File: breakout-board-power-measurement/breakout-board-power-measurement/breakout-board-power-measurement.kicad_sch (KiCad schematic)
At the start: 59 parts, among them J1 Screw_Terminal_01x04, J2 Conn_01x07, J3 Conn_01x07, Q1 NMOS, Q2 NMOS, U1 MCP3911A0-E/SS, U2 Si8641BA-B-IU, U3 LM317_3PinPackage, Y1 10M

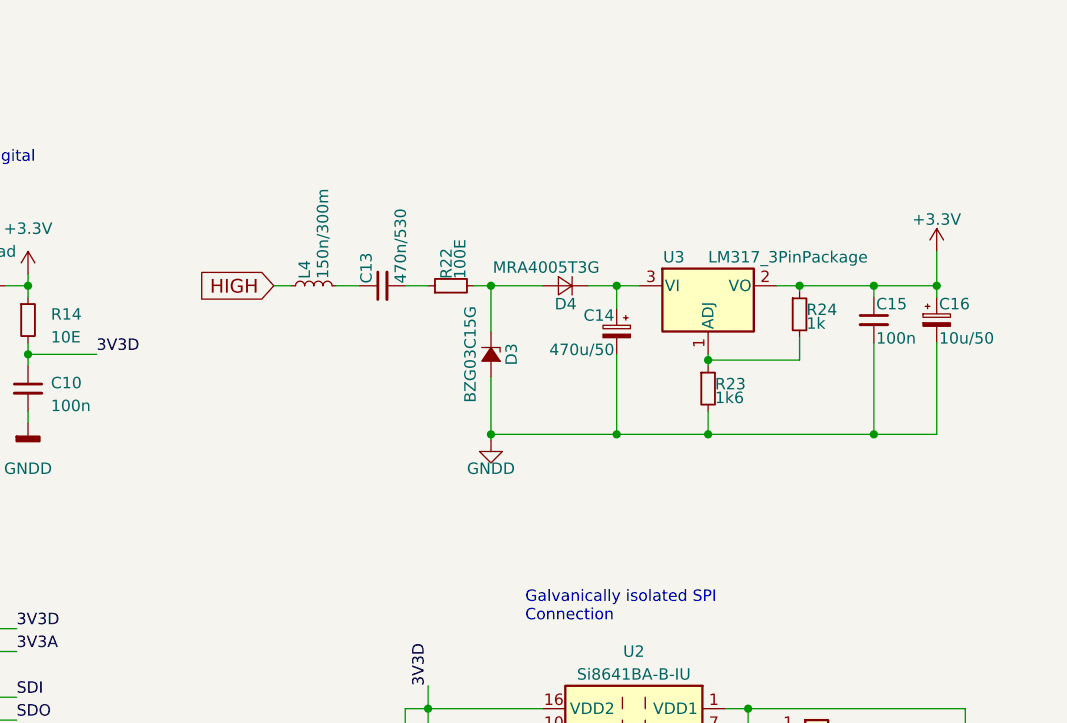
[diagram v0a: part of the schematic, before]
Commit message: LTSpice .raw files wont be uploaded any more. power-measurement breakout will be finished tomorrow
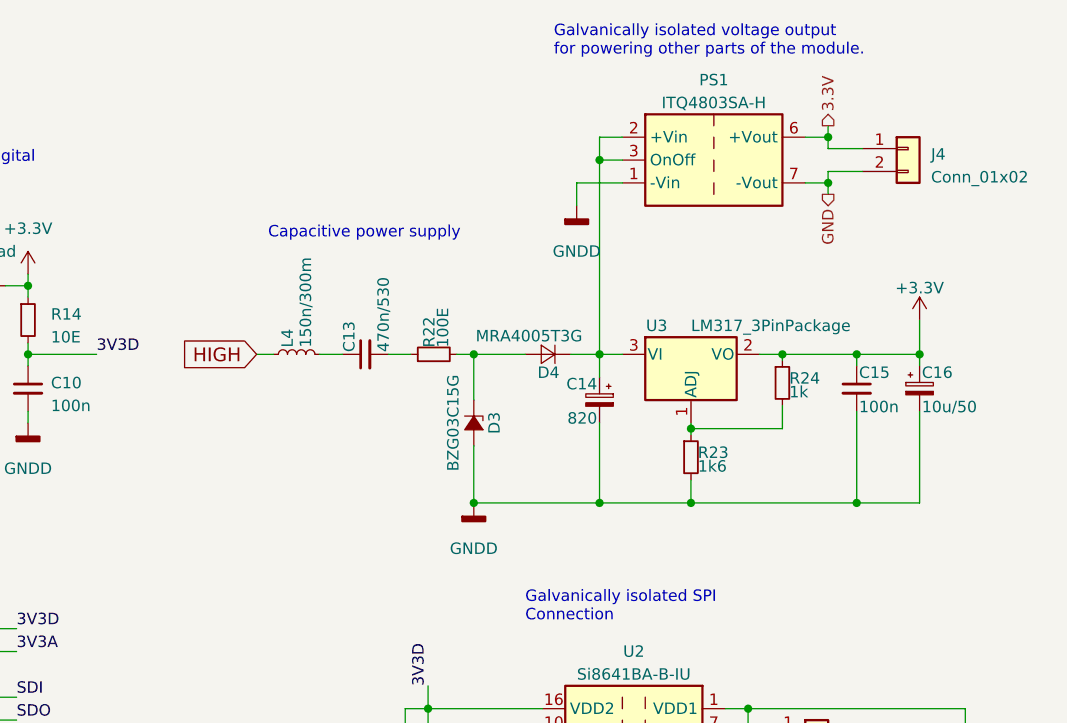
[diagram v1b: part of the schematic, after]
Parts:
- added J4: Conn_01x02, symbol Connector_Generic:Conn_01x02
- added PS1: ITQ4803SA-H, Converter_DCDC:Converter_DCDC_XP_POWER-ITQxxxxS-H_THT, symbol Converter_DCDC:ITQ4803SA-H
- C14: value 470u/50 -> 820
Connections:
- net GNDD: now also PS1.1 (-Vin)
- net at C14.1, D4.1 (K), U3.3 (VI): now also PS1.2 (+Vin), PS1.3 (OnOff)
- new net 3.3V: J4.1 (Pin_1), PS1.6 (+Vout)
- new net GND: J4.2 (Pin_2), PS1.7 (-Vout)
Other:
- note added: "Capacitive power supply"
- note added: "Galvanically isolated voltage output for powering other parts of the module."
- moved on the sheet: C13, C14, C15, C16, D3, D4, L4, R22, R23, R24, U3

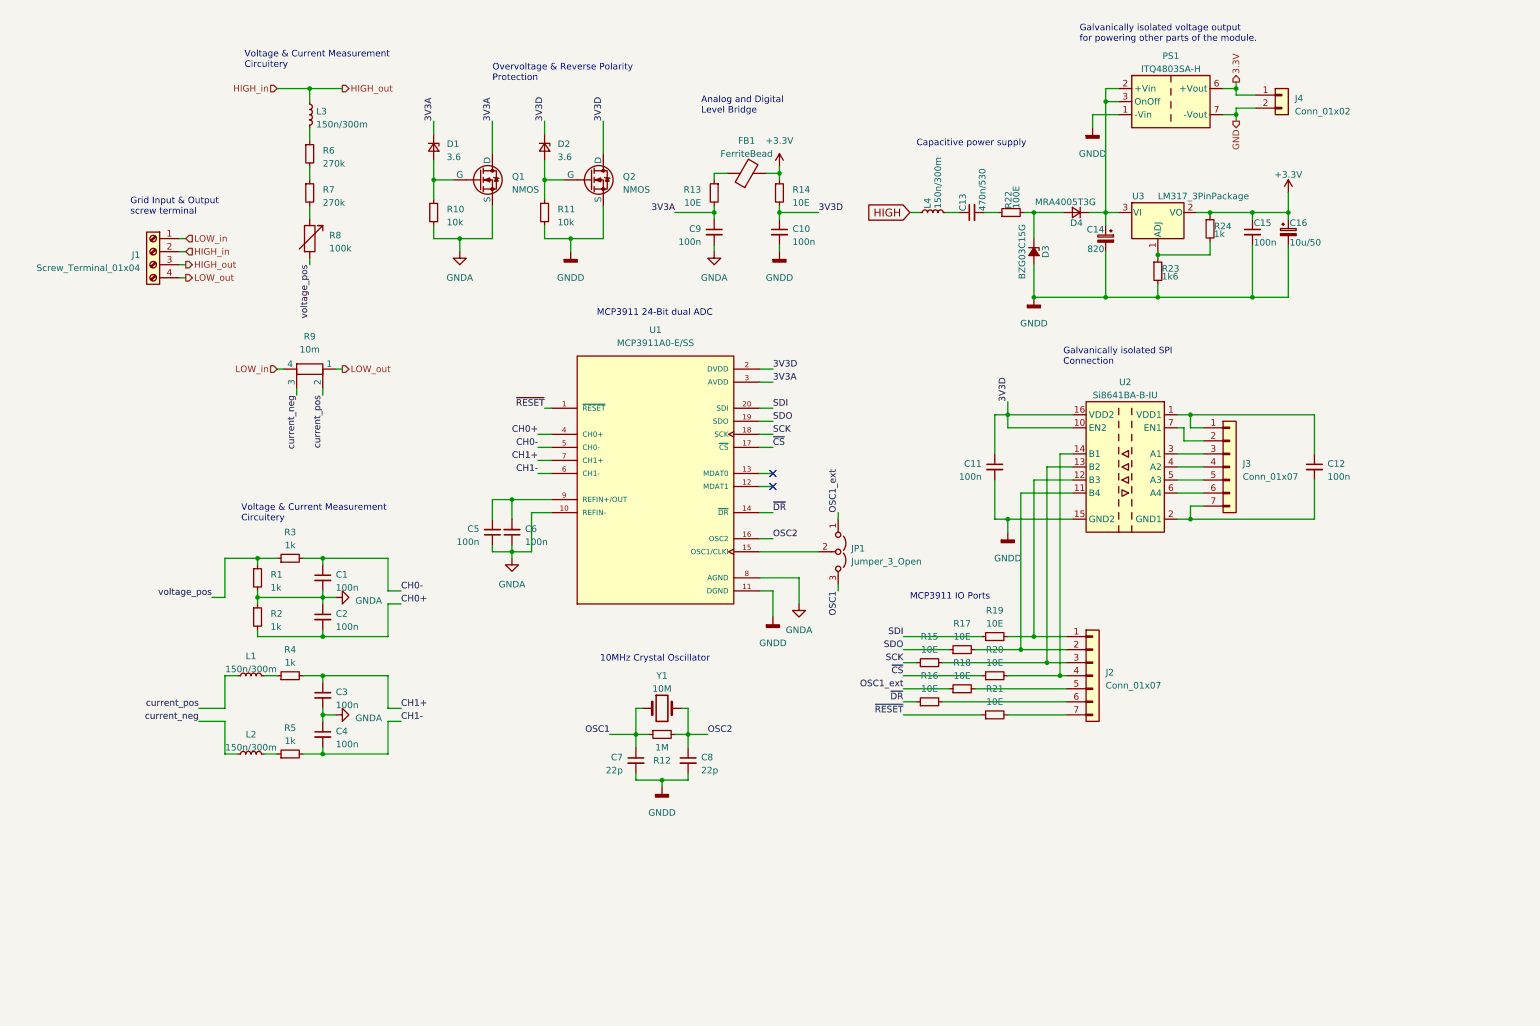
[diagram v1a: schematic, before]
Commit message: power measurement schematic organized
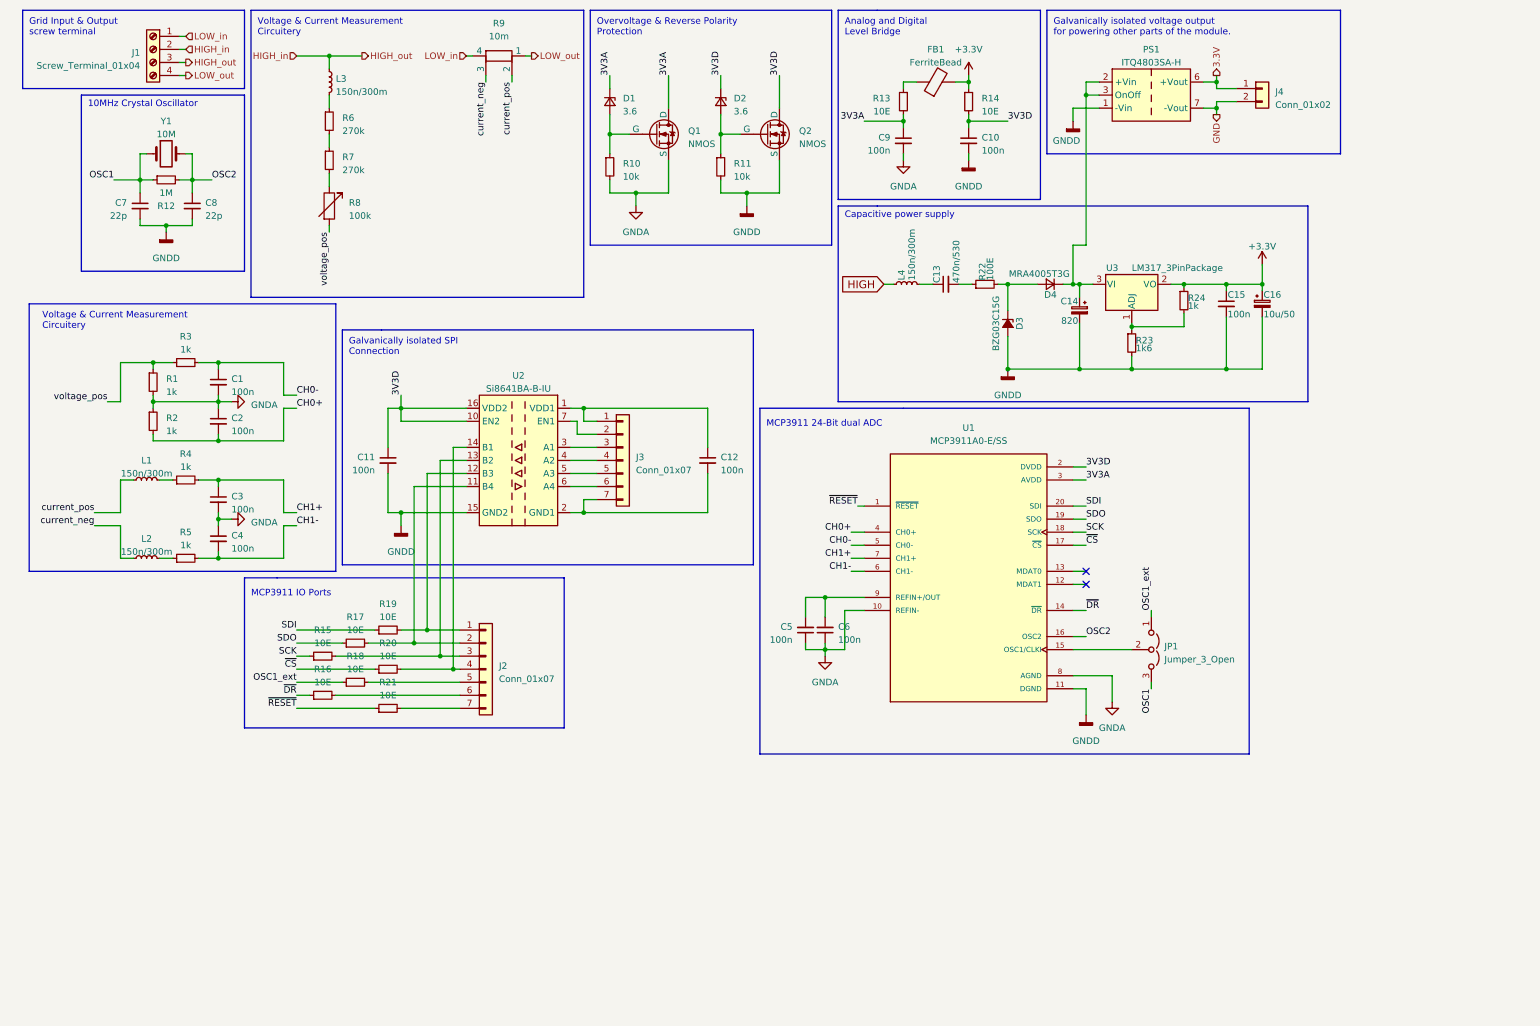
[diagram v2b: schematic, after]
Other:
- moved on the sheet: C1, C10, C11, C12, C13, C14, C15, C16, C2, C3, C4, C5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

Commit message: some footprints added
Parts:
- C1, C10, C11, C12, C2, C3, C4, C5, C6, C7, C8, C9: footprint (none) -> Capacitor_SMD:C_1206_3216Metric_Pad1.33x1.80mm_HandSolder
- J2, J3: footprint (none) -> Connector_PinSocket_2.54mm:PinSocket_1x07_P2.54mm_Vertical
- J4: footprint (none) -> Connector_PinSocket_2.54mm:PinSocket_1x02_P2.54mm_Vertical
- R1, R10, R11, R12, R13, R14, R15, R16, R17, R18, R19, R2, R20, R21, R3, R4, R5, R6, R7, R8: footprint (none) -> Resistor_SMD:R_1206_3216Metric_Pad1.30x1.75mm_HandSolder
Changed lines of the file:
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@@
       (effects (font (size 1.27 1.27)) (justify left))
     )
-    (property "Footprint" "" (at 128.27 44.45 0)
+    (property "Footprint" "Resistor_SMD:R_1206_3216Metric_Pad1.30x1.75mm_HandSolder" (at 128.27 44.45 0)
       (effects (font (size 1.27 1.27)) hide)
     )
@@
       (effects (font (size 1.27 1.27)) (justify left))
     )
-    (property "Footprint" "" (at 185.42 31.75 0)
+    (property "Footprint" "Resistor_SMD:R_1206_3216Metric_Pad1.30x1.75mm_HandSolder" (at 185.42 31.75 0)
       (effects (font (size 1.27 1.27)) hide)
     )
@@
       (effects (font (size 1.27 1.27)) (justify left))
     )
-    (property "Footprint" "" (at 149.86 44.45 0)
+    (property "Footprint" "Resistor_SMD:R_1206_3216Metric_Pad1.30x1.75mm_HandSolder" (at 149.86 44.45 0)
       (effects (font (size 1.27 1.27)) hide)
     )
@@
       (effects (font (size 1.27 1.27)) (justify left))
     )
-    (property "Footprint" "" (at 71.882 52.07 90)
+    (property "Footprint" "Resistor_SMD:R_1206_3216Metric_Pad1.30x1.75mm_HandSolder" (at 71.882 52.07 90)
       (effects (font (size 1.27 1.27)) hide)
     )
@@
       (effects (font (size 1.27 1.27)) (justify right))
     )
-    (property "Footprint" "" (at 170.18 134.62 0)
+    (property "Footprint" "Capacitor_SMD:C_1206_3216Metric_Pad1.33x1.80mm_HandSolder" (at 170.18 134.62 0)
       (effects (font (size 1.27 1.27)) hide)
     )
@@
       (effects (font (size 1.27 1.27)) (justify left))
     )
-    (property "Footprint" "" (at 36.83 52.07 0)
+    (property "Footprint" "Capacitor_SMD:C_1206_3216Metric_Pad1.33x1.80mm_HandSolder" (at 36.83 52.07 0)
       (effects (font (size 1.27 1.27)) hide)
     )
@@
       (effects (font (size 1.27 1.27)))
     )
-    (property "Footprint" "" (at 45.72 105.41 0)
+    (property "Footprint" "Resistor_SMD:R_1206_3216Metric_Pad1.30x1.75mm_HandSolder" (at 45.72 105.41 0)
       (effects (font (size 1.27 1.27)) hide)
     )
@@
       (effects (font (size 1.27 1.27)) (justify left))
     )
-    (property "Footprint" "" (at 73.66 35.56 0)
+    (property "Footprint" "Resistor_SMD:R_1206_3216Metric_Pad1.30x1.75mm_HandSolder" (at 73.66 35.56 0)
       (effects (font (size 1.27 1.27)) hide)
     )
@@
       (effects (font (size 1.27 1.27)) (justify left))
     )
-    (property "Footprint" "" (at 130.81 101.6 0)
+    (property "Footprint" "Connector_PinSocket_2.54mm:PinSocket_1x07_P2.54mm_Vertical" (at 130.81 101.6 0)
       (effects (font (size 1.27 1.27)) hide)
     )
@@
       (effects (font (size 1.27 1.27)) (justify left))
     )
-    (property "Footprint" "" (at 73.66 43.18 0)
+    (property "Footprint" "Resistor_SMD:R_1206_3216Metric_Pad1.30x1.75mm_HandSolder" (at 73.66 43.18 0)
       (effects (font (size 1.27 1.27)) hide)
     )
@@
       (effects (font (size 1.27 1.27)) (justify left))
     )
-    (property "Footprint" "" (at 104.14 142.24 0)
+    (property "Footprint" "Connector_PinSocket_2.54mm:PinSocket_1x07_P2.54mm_Vertical" (at 104.14 142.24 0)
       (effects (font (size 1.27 1.27)) hide)
     )
@@
       (effects (font (size 1.27 1.27)) (justify left))
     )
-    (property "Footprint" "" (at 46.99 52.07 0)
+    (property "Footprint" "Capacitor_SMD:C_1206_3216Metric_Pad1.33x1.80mm_HandSolder" (at 46.99 52.07 0)
       (effects (font (size 1.27 1.27)) hide)
     )
@@
       (effects (font (size 1.27 1.27)) (justify left))
     )
-    (property "Footprint" "" (at 39.37 93.98 0)
+    (property "Footprint" "Resistor_SMD:R_1206_3216Metric_Pad1.30x1.75mm_HandSolder" (at 39.37 93.98 0)
       (effects (font (size 1.27 1.27)) hide)
     )
@@
       (effects (font (size 1.27 1.27)) (justify left))
     )
-    (property "Footprint" "" (at 147.32 101.6 0)
+    (property "Footprint" "Capacitor_SMD:C_1206_3216Metric_Pad1.33x1.80mm_HandSolder" (at 147.32 101.6 0)
       (effects (font (size 1.27 1.27)) hide)
     )
@@
       (effects (font (size 1.27 1.27)))
     )
-    (property "Footprint" "" (at 78.74 137.16 0)
+    (property "Footprint" "Resistor_SMD:R_1206_3216Metric_Pad1.30x1.75mm_HandSolder" (at 78.74 137.16 0)
       (effects (font (size 1.27 1.27)) hide)
     )
@@
       (effects (font (size 1.27 1.27)))
     )
-    (property "Footprint" "" (at 45.72 120.65 0)
+    (property "Footprint" "Resistor_SMD:R_1206_3216Metric_Pad1.30x1.75mm_HandSolder" (at 45.72 120.65 0)
       (effects (font (size 1.27 1.27)) hide)
     )
@@
       (effects (font (size 1.27 1.27)) (justify left))
     )
-    (property "Footprint" "" (at 52.07 86.36 0)
+    (property "Footprint" "Capacitor_SMD:C_1206_3216Metric_Pad1.33x1.80mm_HandSolder" (at 52.07 86.36 0)
       (effects (font (size 1.27 1.27)) hide)
     )
@@
       (effects (font (size 1.27 1.27)) (justify left))
     )
-    (property "Footprint" "" (at 198.12 31.75 0)
+    (property "Footprint" "Resistor_SMD:R_1206_3216Metric_Pad1.30x1.75mm_HandSolder" (at 198.12 31.75 0)
       (effects (font (size 1.27 1.27)) hide)
     )
@@
       (effects (font (size 1.27 1.27)) (justify right))
     )
-    (property "Footprint" "" (at 166.37 134.62 0)
+    (property "Footprint" "Capacitor_SMD:C_1206_3216Metric_Pad1.33x1.80mm_HandSolder" (at 166.37 134.62 0)
       (effects (font (size 1.27 1.27)) hide)
     )
@@
       (effects (font (size 1.27 1.27)) (justify left))
     )
-    (property "Footprint" "" (at 185.42 39.37 0)
+    (property "Footprint" "Capacitor_SMD:C_1206_3216Metric_Pad1.33x1.80mm_HandSolder" (at 185.42 39.37 0)
       (effects (font (size 1.27 1.27)) hide)
     )
@@
       (effects (font (size 1.27 1.27)))
     )
-    (property "Footprint" "" (at 78.74 144.78 0)
+    (property "Footprint" "Resistor_SMD:R_1206_3216Metric_Pad1.30x1.75mm_HandSolder" (at 78.74 144.78 0)
       (effects (font (size 1.27 1.27)) hide)
     )
@@
       (effects (font (size 1.27 1.27)) (justify left))
     )
-    (property "Footprint" "" (at 52.07 116.84 0)
+    (property "Footprint" "Capacitor_SMD:C_1206_3216Metric_Pad1.33x1.80mm_HandSolder" (at 52.07 116.84 0)
       (effects (font (size 1.27 1.27)) hide)
     )
@@
       (effects (font (size 1.27 1.27)) (justify left))
     )
-    (property "Footprint" "" (at 52.07 93.98 0)
+    (property "Footprint" "Capacitor_SMD:C_1206_3216Metric_Pad1.33x1.80mm_HandSolder" (at 52.07 93.98 0)
       (effects (font (size 1.27 1.27)) hide)
     )
@@
       (effects (font (size 1.27 1.27)) (justify left))
     )
-    (property "Footprint" "" (at 39.37 86.36 0)
+    (property "Footprint" "Resistor_SMD:R_1206_3216Metric_Pad1.30x1.75mm_HandSolder" (at 39.37 86.36 0)
       (effects (font (size 1.27 1.27)) hide)
     )
@@
       (effects (font (size 1.27 1.27)))
     )
-    (property "Footprint" "" (at 85.09 134.62 0)
+    (property "Footprint" "Resistor_SMD:R_1206_3216Metric_Pad1.30x1.75mm_HandSolder" (at 85.09 134.62 0)
       (effects (font (size 1.27 1.27)) hide)
     )
@@
       (effects (font (size 1.27 1.27)) (justify left))
     )
-    (property "Footprint" "" (at 255.27 29.21 0)
+    (property "Footprint" "Connector_PinSocket_2.54mm:PinSocket_1x02_P2.54mm_Vertical" (at 255.27 29.21 0)
       (effects (font (size 1.27 1.27)) hide)
     )
@@
       (effects (font (size 1.27 1.27)))
     )
-    (property "Footprint" "" (at 85.09 149.86 0)
+    (property "Footprint" "Resistor_SMD:R_1206_3216Metric_Pad1.30x1.75mm_HandSolder" (at 85.09 149.86 0)
       (effects (font (size 1.27 1.27)) hide)
     )
@@
       (effects (font (size 1.27 1.27)))
     )
-    (property "Footprint" "" (at 41.91 46.99 0)
+    (property "Footprint" "Resistor_SMD:R_1206_3216Metric_Pad1.30x1.75mm_HandSolder" (at 41.91 46.99 0)
       (effects (font (size 1.27 1.27)) hide)
     )
@@
       (effects (font (size 1.27 1.27)))
     )
-    (property "Footprint" "" (at 45.72 82.55 0)
+    (property "Footprint" "Resistor_SMD:R_1206_3216Metric_Pad1.30x1.75mm_HandSolder" (at 45.72 82.55 0)
       (effects (font (size 1.27 1.27)) hide)
     )
@@
       (effects (font (size 1.27 1.27)) (justify left))
     )
-    (property "Footprint" "" (at 198.12 39.37 0)
+    (property "Footprint" "Capacitor_SMD:C_1206_3216Metric_Pad1.33x1.80mm_HandSolder" (at 198.12 39.37 0)
       (effects (font (size 1.27 1.27)) hide)
     )
@@
       (effects (font (size 1.27 1.27)) (justify left))
     )
-    (property "Footprint" "" (at 85.09 101.6 0)
+    (property "Footprint" "Capacitor_SMD:C_1206_3216Metric_Pad1.33x1.80mm_HandSolder" (at 85.09 101.6 0)
       (effects (font (size 1.27 1.27)) hide)
     )
@@
       (effects (font (size 1.27 1.27)) (justify left))
     )
-    (property "Footprint" "" (at 52.07 109.22 0)
+    (property "Footprint" "Capacitor_SMD:C_1206_3216Metric_Pad1.33x1.80mm_HandSolder" (at 52.07 109.22 0)
       (effects (font (size 1.27 1.27)) hide)
     )
@@
       (effects (font (size 1.27 1.27)))
     )
-    (property "Footprint" "" (at 72.39 139.7 0)
+    (property "Footprint" "Resistor_SMD:R_1206_3216Metric_Pad1.30x1.75mm_HandSolder" (at 72.39 139.7 0)
       (effects (font (size 1.27 1.27)) hide)
     )
@@
       (effects (font (size 1.27 1.27)))
     )
-    (property "Footprint" "" (at 72.39 147.32 0)
+    (property "Footprint" "Resistor_SMD:R_1206_3216Metric_Pad1.30x1.75mm_HandSolder" (at 72.39 147.32 0)
       (effects (font (size 1.27 1.27)) hide)
     )
@@
       (effects (font (size 1.27 1.27)))
     )
-    (property "Footprint" "" (at 85.09 142.24 0)
-      (effects (font (size 1.27 1.27)) hide)
-    )
+    (property "Footprint" "Resistor_SMD:R_1206_3216Metric_Pad1.30x1.75mm_HandSolder" (at 85.09 142.24 0)
+      (effects (font (size 1.27 1.27)) hide)
+    )

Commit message: Major updates: Power Measurement PCB-routing half way done.
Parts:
- added U4: LM2575-3.3BT, Package_TO_SOT_THT:TO-220-5_Vertical, symbol Regulator_Switching:LM2575-3.3BT
- JP1: footprint (none) -> Pin_Headers:Pin_Header_Straight_1x03_Pitch2.54mm
- L1, L2, L3: footprint (none) -> Inductors_SMD:L_1206_HandSoldering
- R9: footprint (none) -> Resistors_THT:R_Axial_DIN0516_L15.5mm_D5.0mm_P20.32mm_Horizontal
- U1: footprint (none) -> Housings_SSOP:SSOP-20_5.3x7.2mm_Pitch0.65mm
- Y1: footprint (none) -> Crystals:Crystal_HC49-4H_Vertical
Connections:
- net GNDD: now also U4.3 (GND), U4.5 (~{ON}/OFF); no longer PS1.1 (-Vin)
- net at C14.1, D4.1 (K), U3.3 (VI): now also U4.1 (VIN); no longer PS1.2 (+Vin), PS1.3 (OnOff)
- new net: PS1.1 (-Vin), U4.2 (OUT)
- new net: PS1.2 (+Vin), PS1.3 (OnOff), U4.4 (FB)
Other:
- note added: "Power output for ADC"
- moved on the sheet: C1, C10, C11, C12, C13, C14, C15, C16, C2, C3, C4, C5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
